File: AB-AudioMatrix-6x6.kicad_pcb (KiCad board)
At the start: 4 copper layers, 200 x 70 mm, 83 parts, among them J1 Switchcraft-35RAPC4BH3, J10 Switchcraft-35RAPC4BH3, J11 Switchcraft-35RAPC4BH3, J12 Switchcraft-35RAPC4BH3, J13 Conn_01x24, J14 Conn_01x24, J15 Screw_Terminal_01x03, J16 Conn_01x24, J17 Conn_01x24, J2 Switchcraft-35RAPC4BH3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

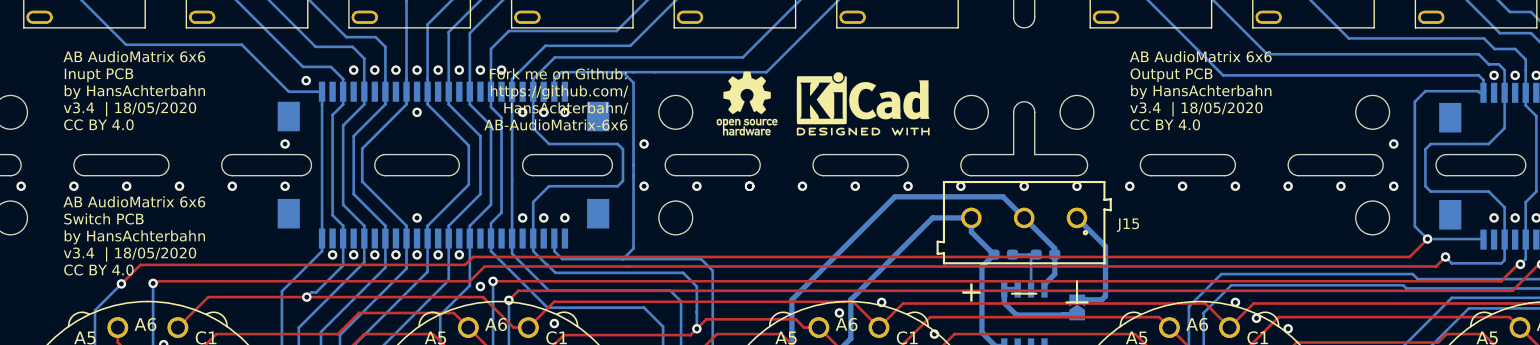
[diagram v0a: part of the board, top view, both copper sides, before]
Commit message: added new attributes MF, MFN, Mouser, Digi-Key, RS-Online, Infopage, datasheet | bill of material (BOM) created | infobox updated | added AudioBürokrat logo on silkscreen
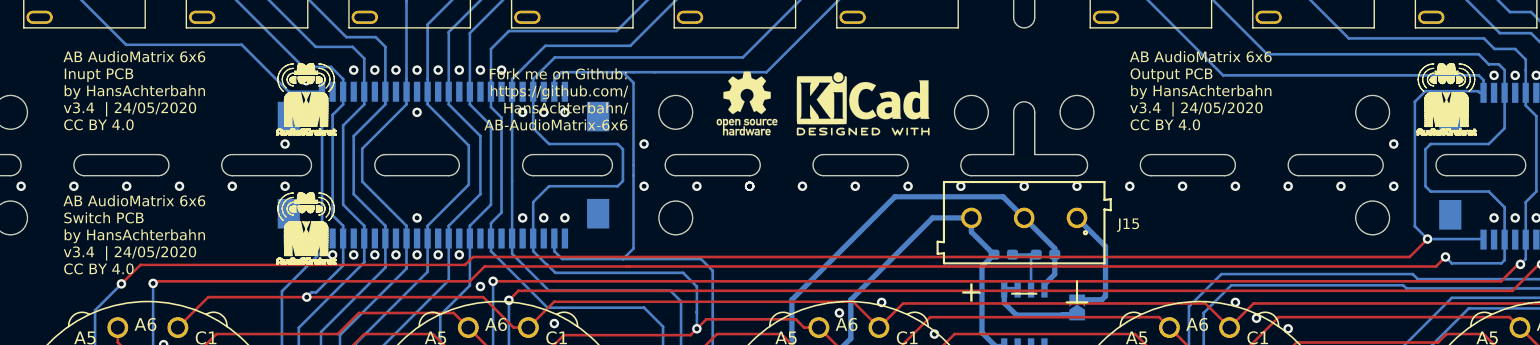
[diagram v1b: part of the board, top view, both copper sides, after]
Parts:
- added REF**: AudioBürokrat-6mm-font, h8-Logos:AudioBürokrat-6mm-font, F.Cu at (183.0, 99.1)
- added REF**: AudioBürokrat-6mm-font, h8-Logos:AudioBürokrat-6mm-font, F.Cu at (75.0, 99.1)
- added REF**: AudioBürokrat-6mm-font, h8-Logos:AudioBürokrat-6mm-font, F.Cu at (75.0, 111.3)
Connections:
- net +9V renamed +VDC
- net -9V renamed -VDC
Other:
- board text added: "AB AudioMatrix 6x6 Inupt PCB by HansAchterbahn v3.4 | 24/05/2020 CC BY 4.0"
- board text added: "AB AudioMatrix 6x6 Output PCB by HansAchterbahn v3.4 | 24/05/2020 CC BY 4.0"
- board text added: "AB AudioMatrix 6x6 Switch PCB by HansAchterbahn v3.4 | 24/05/2020 CC BY 4.0"
- board text removed: "AB AudioMatrix 6x6 Inupt PCB by HansAchterbahn v3.4 | 18/05/2020 CC BY 4.0"
- board text removed: "AB AudioMatrix 6x6 Output PCB by HansAchterbahn v3.4 | 18/05/2020 CC BY 4.0"
- board text removed: "AB AudioMatrix 6x6 Switch PCB by HansAchterbahn v3.4 | 18/05/2020 CC BY 4.0"

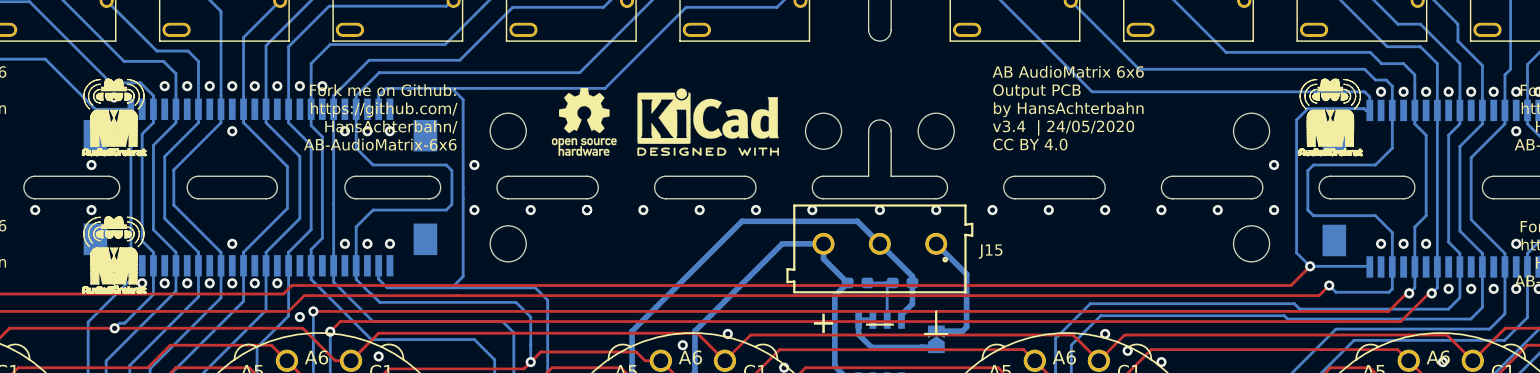
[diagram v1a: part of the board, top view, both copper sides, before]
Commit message: changed AudioBürokrat logo
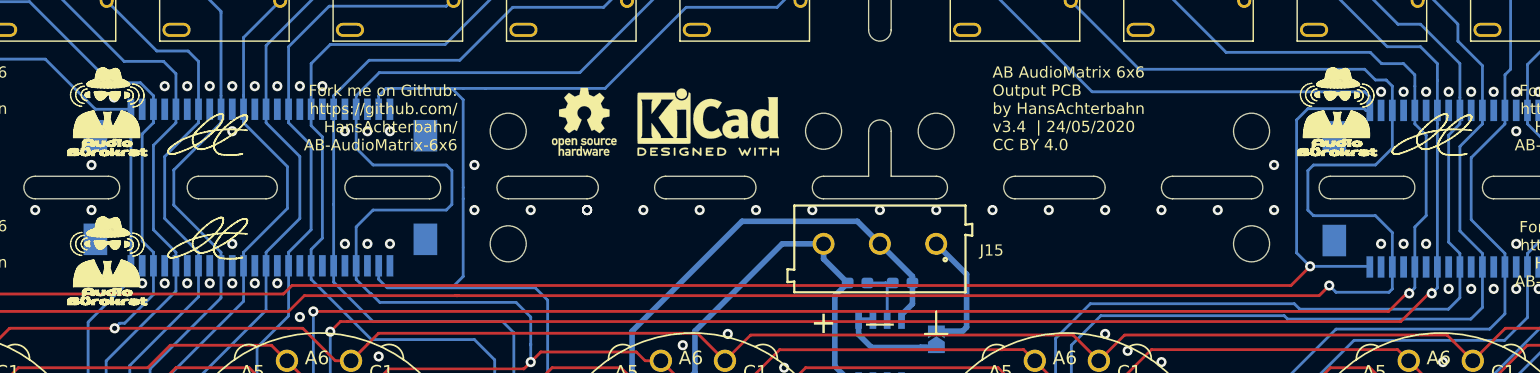
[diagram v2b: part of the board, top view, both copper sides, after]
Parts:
- removed the REF** at (183.0, 99.1)
- removed the REF** at (75.0, 99.1)
- removed the REF** at (75.0, 111.3)
- added REF**: AudioBürokrat02-8mm, h8-Logos:AudioBürokrat02-8mm, F.Cu at (74.4, 111.9)
- added REF**: AudioBürokrat02-8mm, h8-Logos:AudioBürokrat02-8mm, F.Cu at (74.4, 98.6)
- added REF**: h8-Logo-4mm, h8-Logos:h8-Logo-4mm, F.Cu at (84.0, 100.5)
- added REF**: AudioBürokrat02-8mm, h8-Logos:AudioBürokrat02-8mm, F.Cu at (183.6, 98.6)
- added REF**: h8-Logo-4mm, h8-Logos:h8-Logo-4mm, F.Cu at (192.7, 100.5)
- added REF**: h8-Logo-4mm, h8-Logos:h8-Logo-4mm, F.Cu at (84.0, 109.7)

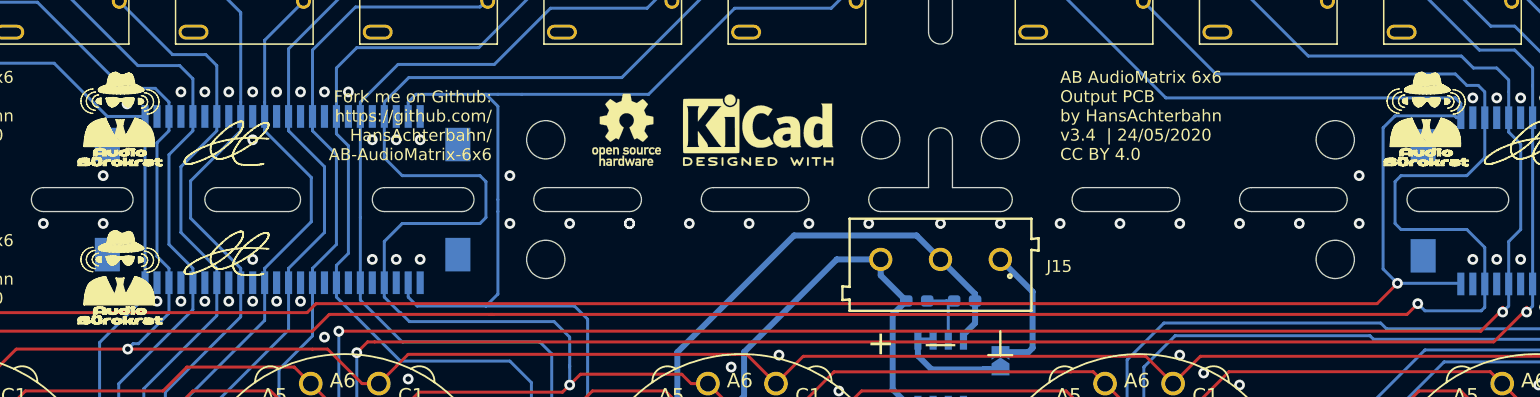
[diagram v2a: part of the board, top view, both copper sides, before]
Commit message: changed AudioBürokrat logo (Bitmap import)
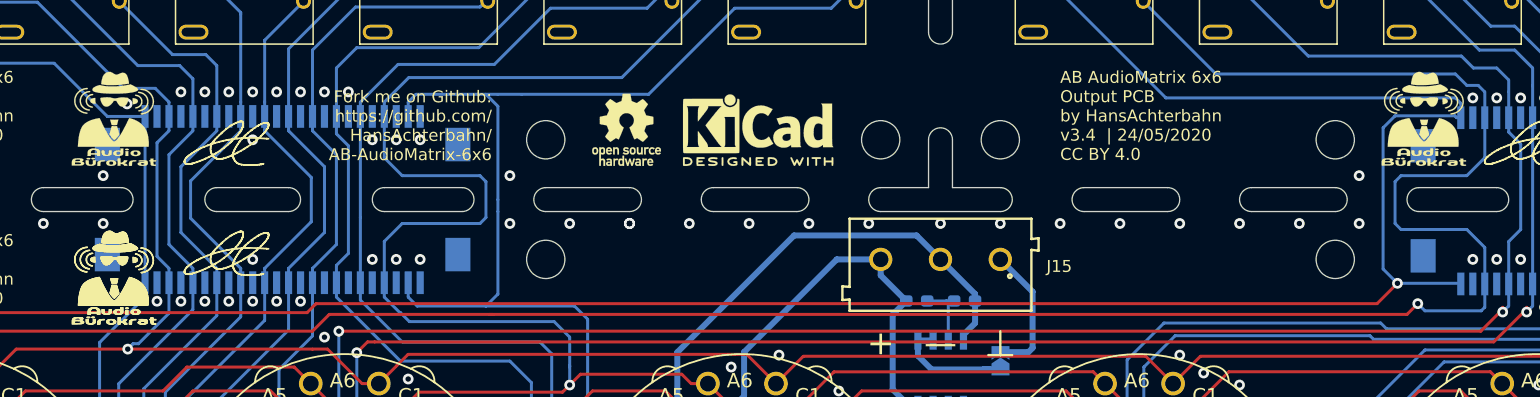
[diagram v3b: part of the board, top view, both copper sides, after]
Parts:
- removed the REF** at (74.4, 111.9)
- removed the REF** at (74.4, 98.6)
- removed the REF** at (183.6, 98.6)
- added G***: AudioBürokrat-Logo-8mm, h8-Logos:AudioBürokrat-Logo-8mm, F.Cu at (183.4, 98.3)
- added G***: AudioBürokrat-Logo-8mm, h8-Logos:AudioBürokrat-Logo-8mm, F.Cu at (73.9, 98.3)
- added G*** (x2): AudioBürokrat-Logo-8mm, h8-Logos:AudioBürokrat-Logo-8mm, F.Cu at (73.9, 111.5)
